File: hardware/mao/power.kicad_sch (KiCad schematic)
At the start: 36 parts, among them J101 USB-C, J102 BAT, Q101 AO3401A, U101 TPD2E2U06, U102 BQ24073RGTR, U103 MAX17048G+T10, U104 TPS63802DLAR, U105 TPS22919DCKR

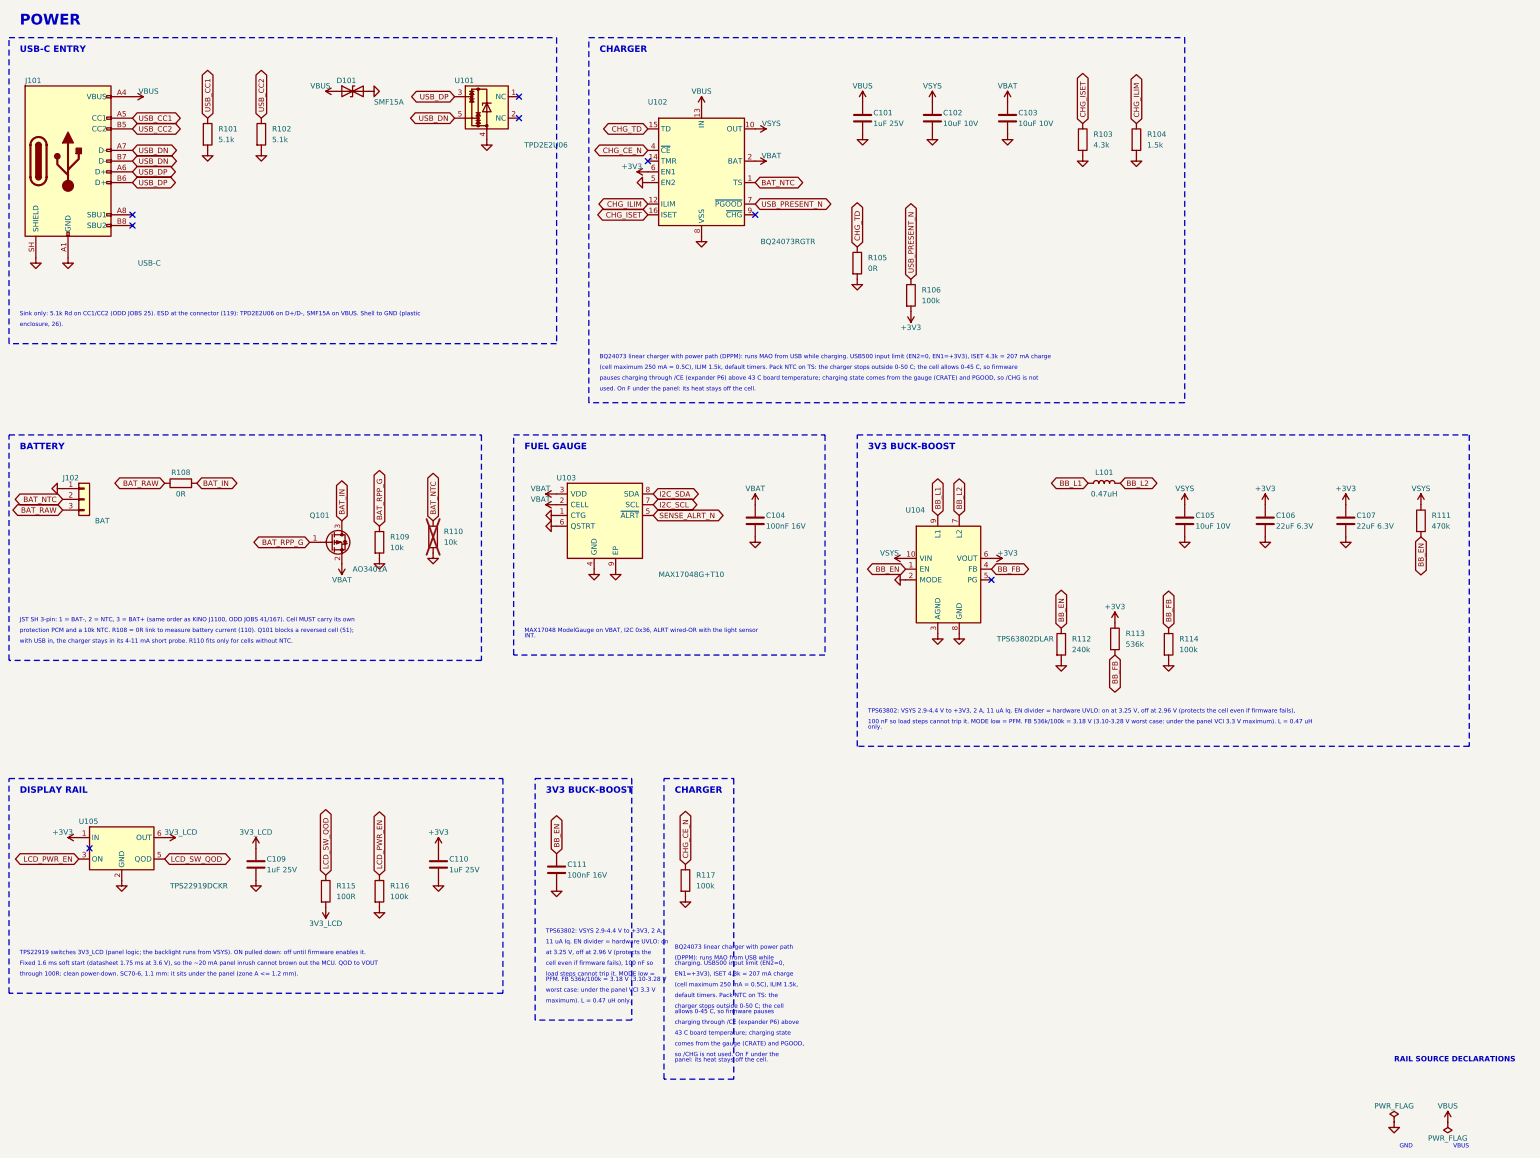
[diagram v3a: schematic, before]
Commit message: MAO A0 schematic: one frame per block, wired local nets, no overprinted names
ODD JOBS audit 2, X8 (rules 187, 188):
- Parts added late (C111, R117, R507) join their block's frame instead of opening a duplicate frame
  with a copy of its note that ran over the neighbours.
- A two-pin part on a net that only joins it to one side pin of its block's IC is wired to that pin
  (the pin's label still names the net, so board, rules and procedures keep their names); feedback and
  UVLO-style dividers hang off their pin as a divider column. Columns step so no wire crosses a part.
- Adjacent pins on one rail share one rail symbol, joined by a wire; a sideways rail symbol keeps its
  name on its own row; turned passives, LEDs and diodes keep their reference and value off the body.
- Rail-source declarations sit in their own frame in the layout flow, not over the title block.
- Two stale notes corrected (C105 distance to VIN, R204 A0 voltage); board fields synced.

ERC 0, DRC 0 / 0 / parity 0.

Co-Authored-By: Claude Opus 5.5 <noreply@anthropic.com>
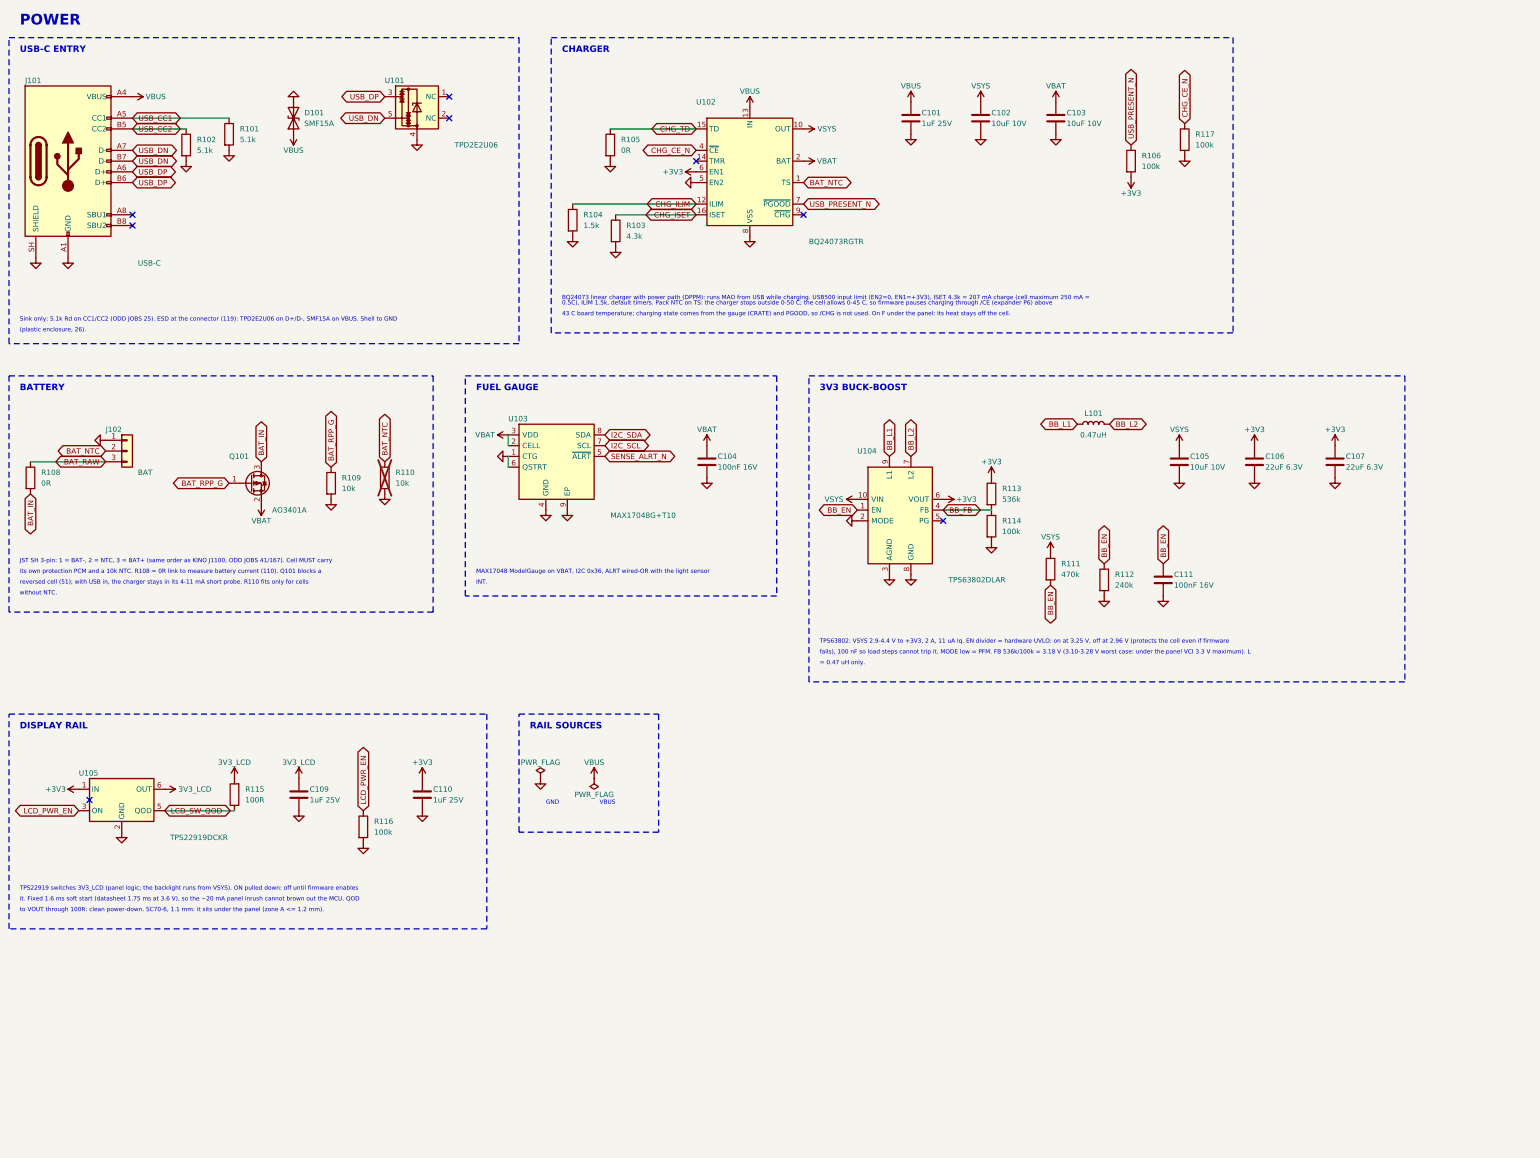
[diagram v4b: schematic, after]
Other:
- note added: "(plastic enclosure, 26)."
- note added: "0.5C), ILIM 1.5k, default timers. Pack NTC on TS: the charger stops outside 0-50 C; the cell allows 0-45 C, so firmware pauses charging through /CE (expander P6) above"
- note added: "43 C board temperature; charging state comes from the gauge (CRATE) and PGOOD, so /CHG is not used. On F under the panel: its heat stays off the cell."
- note added: "= 0.47 uH only."
- note added: "BQ24073 linear charger with power path (DPPM): runs MAO from USB while charging. USB500 input limit (EN2=0, EN1=+3V3), ISET 4.3k = 207 mA charge (cell maximum 250 mA ="
- note added: "JST SH 3-pin: 1 = BAT-, 2 = NTC, 3 = BAT+ (same order as KINO J1100, ODD JOBS 41/167). Cell MUST carry"
- note added: "RAIL SOURCES"
- note added: "Sink only: 5.1k Rd on CC1/CC2 (ODD JOBS 25). ESD at the connector (119): TPD2E2U06 on D+/D-, SMF15A on VBUS. Shell to GND"
- note added: "TPS22919 switches 3V3_LCD (panel logic; the backlight runs from VSYS). ON pulled down: off until firmware enables"
- note added: "TPS63802: VSYS 2.9-4.4 V to +3V3, 2 A, 11 uA Iq. EN divider = hardware UVLO: on at 3.25 V, off at 2.96 V (protects the cell even if firmware"
- note added: "fails), 100 nF so load steps cannot trip it. MODE low = PFM. FB 536k/100k = 3.18 V (3.10-3.28 V worst case: under the panel VCI 3.3 V maximum). L"
- note added: "it. Fixed 1.6 ms soft start (datasheet 1.75 ms at 3.6 V), so the ~20 mA panel inrush cannot brown out the MCU. QOD"
- note added: "its own protection PCM and a 10k NTC. R108 = 0R link to measure battery current (110). Q101 blocks a"
- note added: "reversed cell (51); with USB in, the charger stays in its 4-11 mA short probe. R110 fits only for cells"
- note added: "to VOUT through 100R: clean power-down. SC70-6, 1.1 mm: it sits under the panel (zone A <= 1.2 mm)."
- note added: "without NTC."
- note removed: "(DPPM): runs MAO from USB while"
- note removed: "(cell maximum 250 mA = 0.5C), ILIM 1.5k,"
- note removed: "(cell maximum 250 mA = 0.5C), ILIM 1.5k, default timers. Pack NTC on TS: the charger stops outside 0-50 C; the cell allows 0-45 C, so firmware"
- note removed: "100 nF so load steps cannot trip it. MODE low = PFM. FB 536k/100k = 3.18 V (3.10-3.28 V worst case: under the panel VCI 3.3 V maximum). L = 0.47 uH"
- note removed: "11 uA Iq. EN divider = hardware UVLO: on"
- note removed: "43 C board temperature; charging state"
- note removed: "BQ24073 linear charger with power path"
- note removed: "BQ24073 linear charger with power path (DPPM): runs MAO from USB while charging. USB500 input limit (EN2=0, EN1=+3V3), ISET 4.3k = 207 mA charge"
- note removed: "EN1=+3V3), ISET 4.3k = 207 mA charge"
- note removed: "Fixed 1.6 ms soft start (datasheet 1.75 ms at 3.6 V), so the ~20 mA panel inrush cannot brown out the MCU. QOD to VOUT"
- note removed: "JST SH 3-pin: 1 = BAT-, 2 = NTC, 3 = BAT+ (same order as KINO J1100, ODD JOBS 41/167). Cell MUST carry its own"
- note removed: "PFM. FB 536k/100k = 3.18 V (3.10-3.28 V"
- note removed: "RAIL SOURCE DECLARATIONS"
- note removed: "Sink only: 5.1k Rd on CC1/CC2 (ODD JOBS 25). ESD at the connector (119): TPD2E2U06 on D+/D-, SMF15A on VBUS. Shell to GND (plastic"
- note removed: "TPS22919 switches 3V3_LCD (panel logic; the backlight runs from VSYS). ON pulled down: off until firmware enables it."
- note removed: "TPS63802: VSYS 2.9-4.4 V to +3V3, 2 A,"
- note removed: "TPS63802: VSYS 2.9-4.4 V to +3V3, 2 A, 11 uA Iq. EN divider = hardware UVLO: on at 3.25 V, off at 2.96 V (protects the cell even if firmware fails),"
- note removed: "allows 0-45 C, so firmware pauses"
- note removed: "at 3.25 V, off at 2.96 V (protects the"
- note removed: "cell even if firmware fails), 100 nF so"
- note removed: "charger stops outside 0-50 C; the cell"
- note removed: "charging through /CE (expander P6) above"
- note removed: "charging. USB500 input limit (EN2=0,"
- note removed: "comes from the gauge (CRATE) and PGOOD,"
- note removed: "default timers. Pack NTC on TS: the"
- note removed: "enclosure, 26)."
- note removed: "load steps cannot trip it. MODE low ="
- note removed: "maximum). L = 0.47 uH only."
- note removed: "only."
- note removed: "panel: its heat stays off the cell."
- note removed: "pauses charging through /CE (expander P6) above 43 C board temperature; charging state comes from the gauge (CRATE) and PGOOD, so /CHG is not"
- note removed: "protection PCM and a 10k NTC. R108 = 0R link to measure battery current (110). Q101 blocks a reversed cell (51);"
- note removed: "so /CHG is not used. On F under the"
- note removed: "through 100R: clean power-down. SC70-6, 1.1 mm: it sits under the panel (zone A <= 1.2 mm)."
- note removed: "used. On F under the panel: its heat stays off the cell."
- note removed: "with USB in, the charger stays in its 4-11 mA short probe. R110 fits only for cells without NTC."
- note removed: "worst case: under the panel VCI 3.3 V"
- moved on the sheet: C101, C102, C103, C104, C105, C106, C107, C109, C110, C111, D101, J102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

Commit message: MAO A0 audit 3 fixes: VSYS feed un-necked, speaker lines over VSYS, silk leaders to their parts
Electrical audit 3 (no blocker; issue I-1):
- 11 o'clock panel tab 320 -> 328 deg: its keep-out necked the L3 VSYS band to 0.27 mm beside H1
- via-free corner where the VSYS branch turns into the backlight bar (a C205/U202 via left 0.26 mm)
- plane_check: GND and rail regions refilled at 0.5 mm minimum width must not split (necks fail
  the build); the +3V3 mesh is reported
- self-test board_id upper limit 1700 -> 1720 mV (the 3.32 V rail corner reached 1.697 V)
- comments: rail 3.10-3.32 V, AW9364 dropout, TPS22919 turn-on vs rise, panel clock, Kconfig help
- D101 drawn as a unidirectional TVS (zener glyph); module +3V3 via on C202's branch axis

ODD JOBS audit 3 (0 FAIL; recommended fixes):
- VSYS branch extended under both speaker lines (they sat over the VSYS/+3V3 zone gap); LCD_RST_N
  off L3; L3/L4 broadside 17.4 -> 13.8 mm
- EXP_RST_N's leg to TP11 designed on L3 (left to the router it detoured)
- leaders end 0.3 mm off their own part, at least 0.1 mm nearer it than any other part
- no silk text on touch-electrode copper (silk.py, mao_labels.py, check_silk_text.py): REAR and
  MIC moved
- schematic note lines on a 2.54 mm pitch (snapped 2.29 mm printed pairs that touched); tail note
- back identity on a reserved via-free spot; RSSI check with and without the LRA; drawing text
- final board: DRC 0/0/0, planes whole, no rail neck under 0.5 mm, silk 83 texts 0 findings,
  mech 0, 205 vias, 921 segments on 45 degrees; firmware 5 builds 0 warnings, 240 host checks;
  merge patch re-verified on b17187e

Co-Authored-By: Claude Opus 5.5 <noreply@anthropic.com>
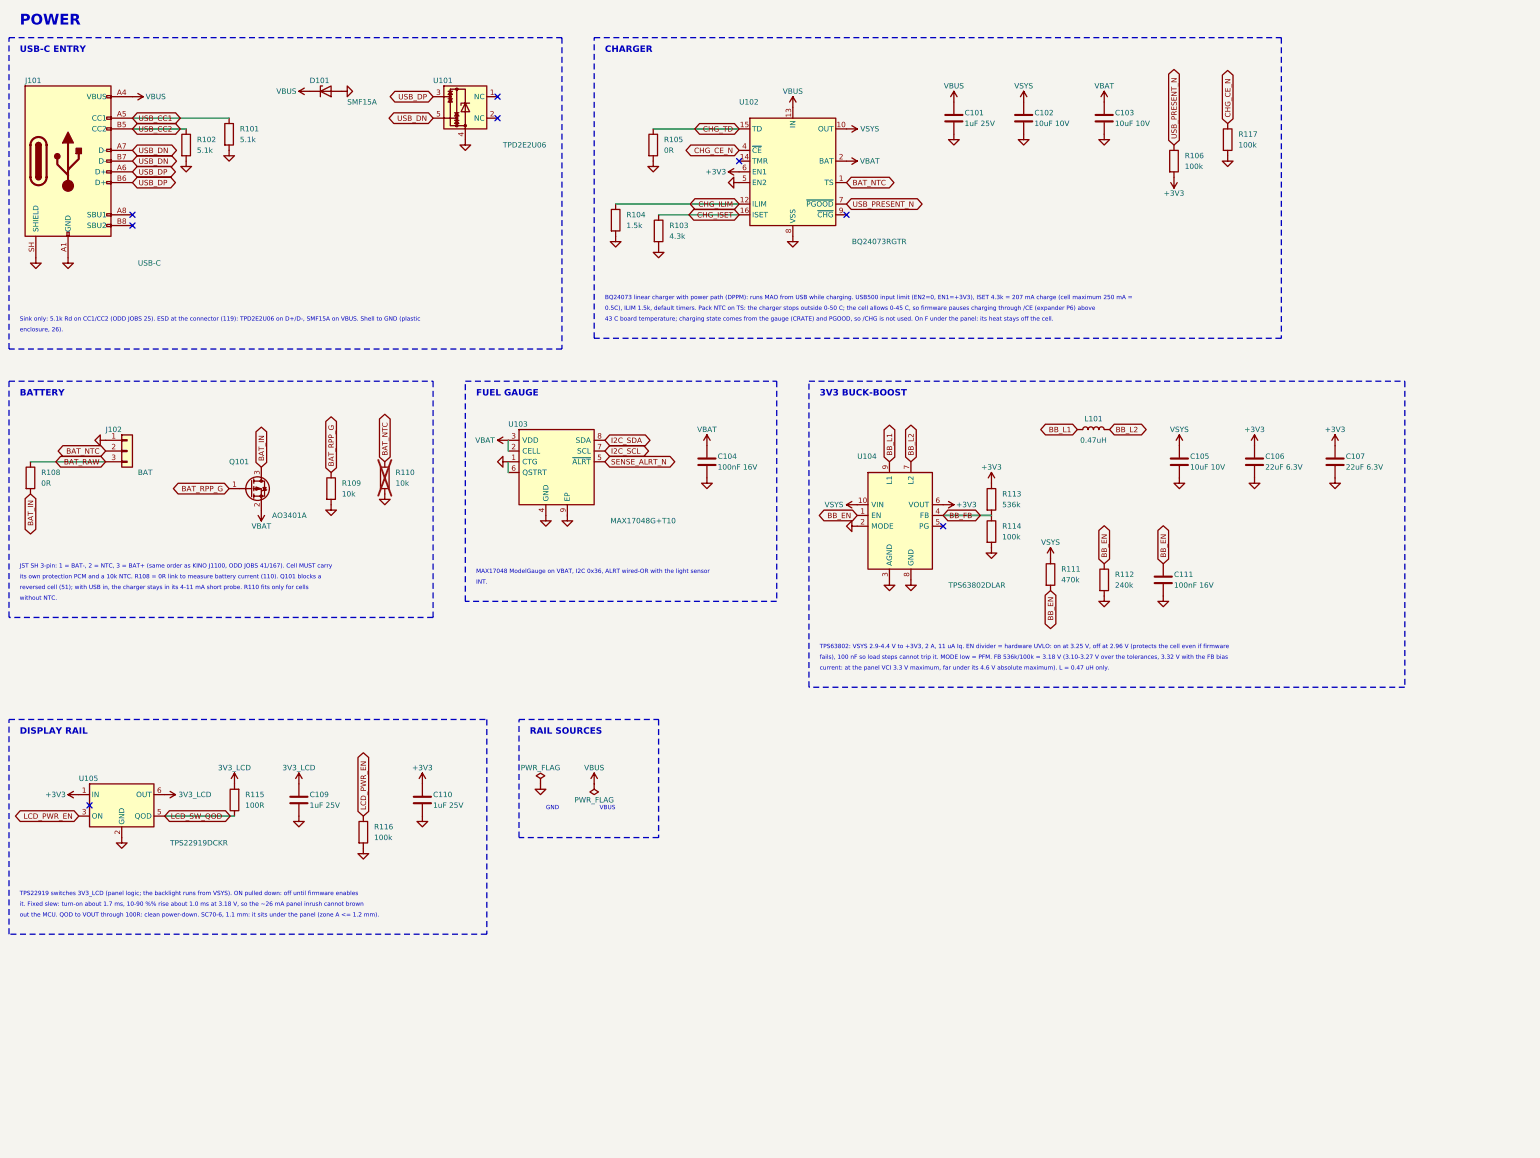
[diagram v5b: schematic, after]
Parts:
- D101: symbol Device:D_TVS -> Device:D_Zener
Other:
- note added: "Sink only: 5.1k Rd on CC1/CC2 (ODD JOBS 25). ESD at the connector (119): TPD2E2U06 on D+/D-, SMF15A on VBUS. Shell to GND (plastic"
- note added: "current: at the panel VCI 3.3 V maximum, far under its 4.6 V absolute maximum). L = 0.47 uH only."
- note added: "enclosure, 26)."
- note added: "fails), 100 nF so load steps cannot trip it. MODE low = PFM. FB 536k/100k = 3.18 V (3.10-3.27 V over the tolerances, 3.32 V with the FB bias"
- note added: "it. Fixed slew: turn-on about 1.7 ms, 10-90 %% rise about 1.0 ms at 3.18 V, so the ~26 mA panel inrush cannot brown"
- note added: "out the MCU. QOD to VOUT through 100R: clean power-down. SC70-6, 1.1 mm: it sits under the panel (zone A <= 1.2 mm)."
- note removed: "(plastic enclosure, 26)."
- note removed: "= 0.47 uH only."
- note removed: "Sink only: 5.1k Rd on CC1/CC2 (ODD JOBS 25). ESD at the connector (119): TPD2E2U06 on D+/D-, SMF15A on VBUS. Shell to GND"
- note removed: "fails), 100 nF so load steps cannot trip it. MODE low = PFM. FB 536k/100k = 3.18 V (3.10-3.28 V worst case: under the panel VCI 3.3 V maximum). L"
- note removed: "it. Fixed 1.6 ms soft start (datasheet 1.75 ms at 3.6 V), so the ~20 mA panel inrush cannot brown out the MCU. QOD"
- note removed: "to VOUT through 100R: clean power-down. SC70-6, 1.1 mm: it sits under the panel (zone A <= 1.2 mm)."
- moved on the sheet: C101, C102, C103, C109, C110, D101, L101, Q101, R103, R104, R105, R106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
